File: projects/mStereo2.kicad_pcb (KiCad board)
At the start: 4 copper layers, 159.5 x 120 mm, 125 parts, among them P101 CONN_AMANERO, P102 Screw-term 1x2, P103 Screw-term 1X3, P104 XLR-MALE, P105 XLR-MALE, U101 ISO7640, U102 CDCLVC1104, U103 MCP100-315DI, U104 SRC4192, U201 LT1761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

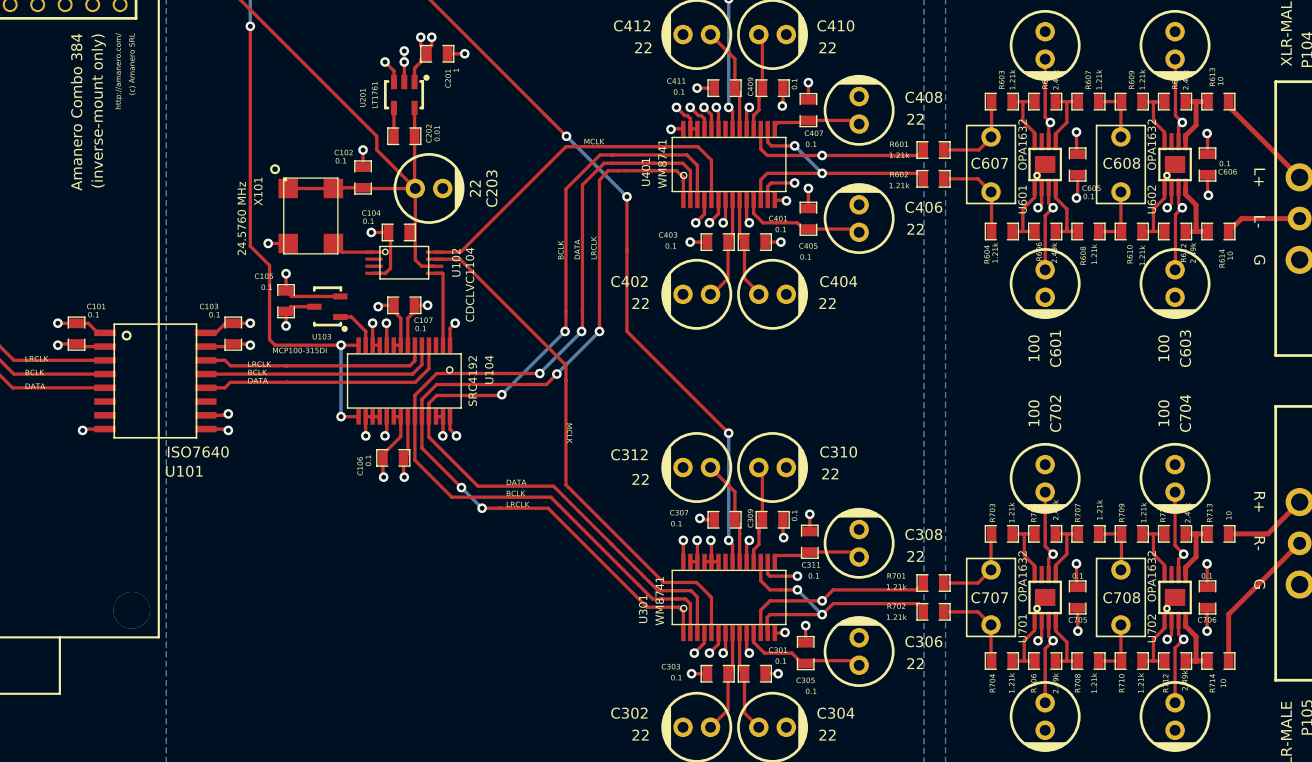
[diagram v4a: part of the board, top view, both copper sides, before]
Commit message: finalize silkscreen, ran DRC, did layer-by-layer visual sanity-check
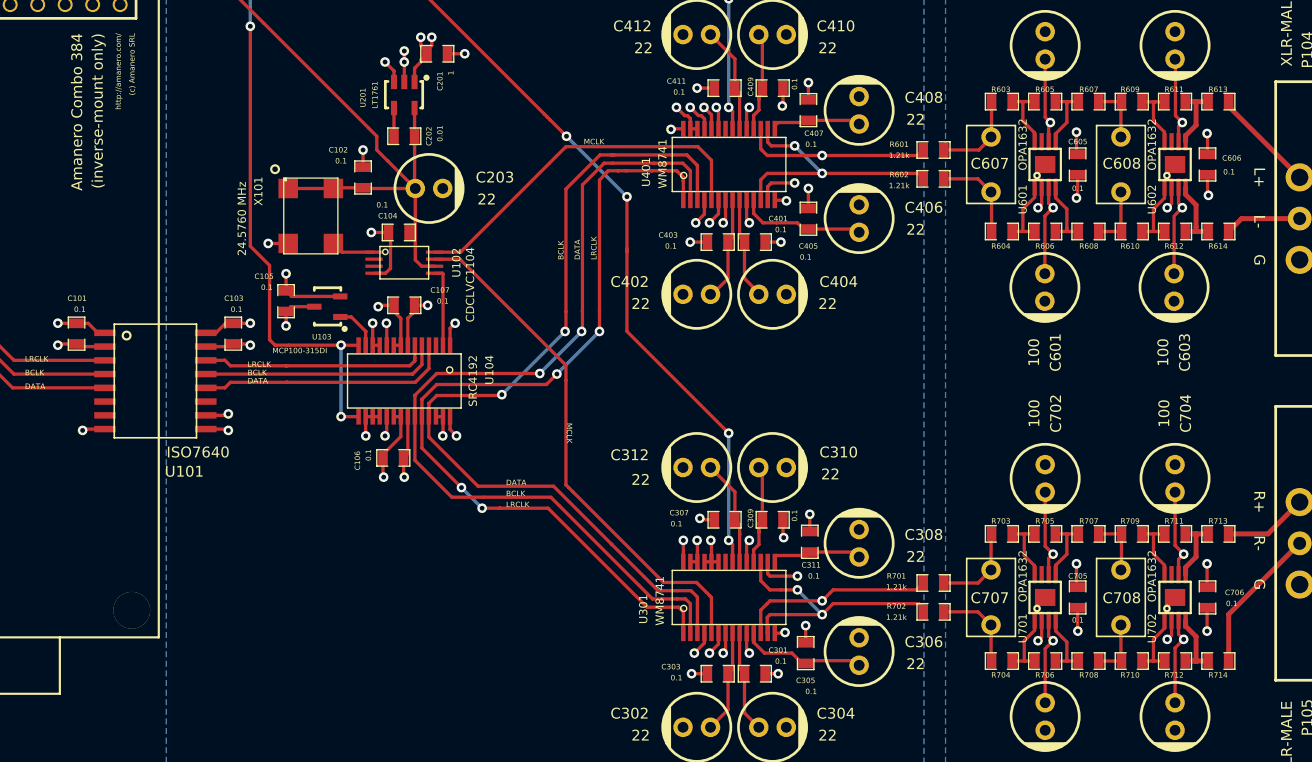
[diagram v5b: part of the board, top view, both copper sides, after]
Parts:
- moved C603 0.37 mm to (166.1, 86.4)
- moved C601 0.36 mm to (154.2, 86.4)
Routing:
- net +12V: track 106.0 -> 106.6 mm
